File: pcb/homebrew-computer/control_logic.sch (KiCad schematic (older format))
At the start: 24 parts

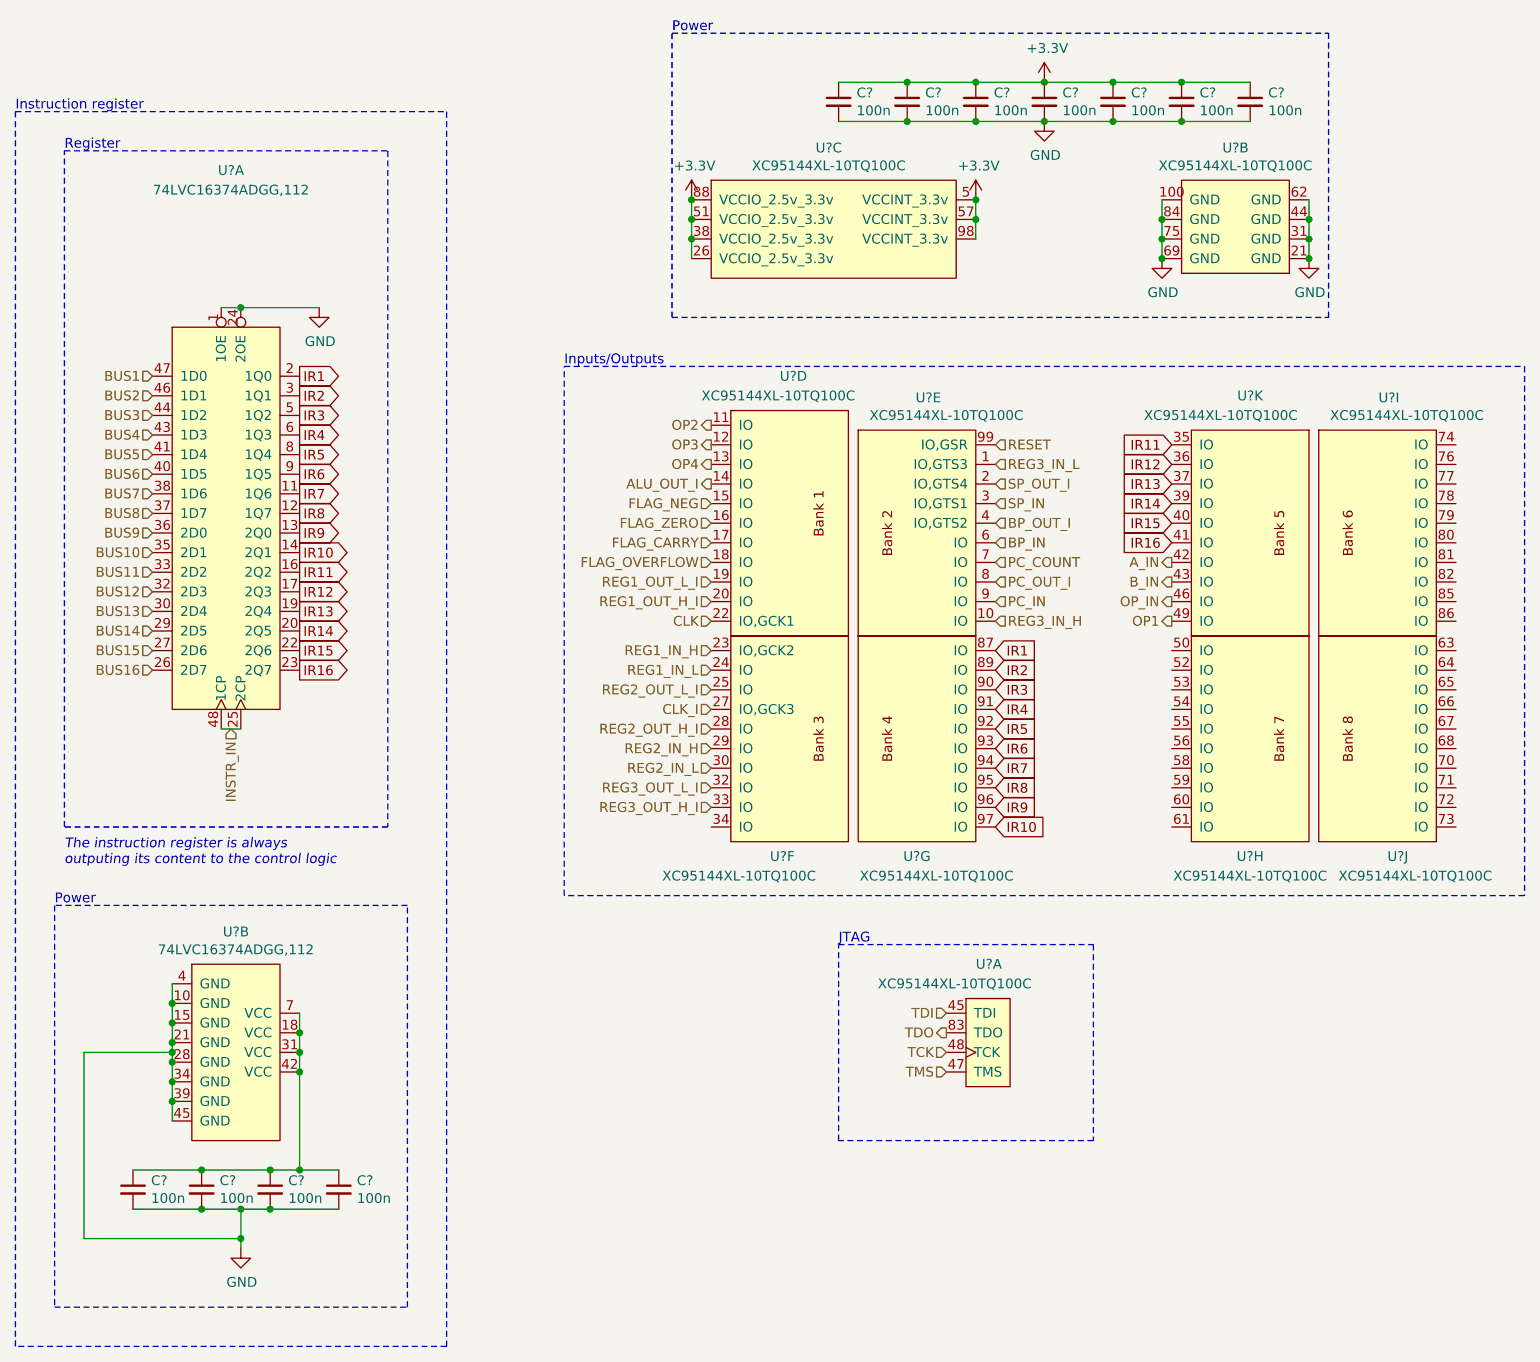
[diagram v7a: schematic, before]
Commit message: Connect signals between modules
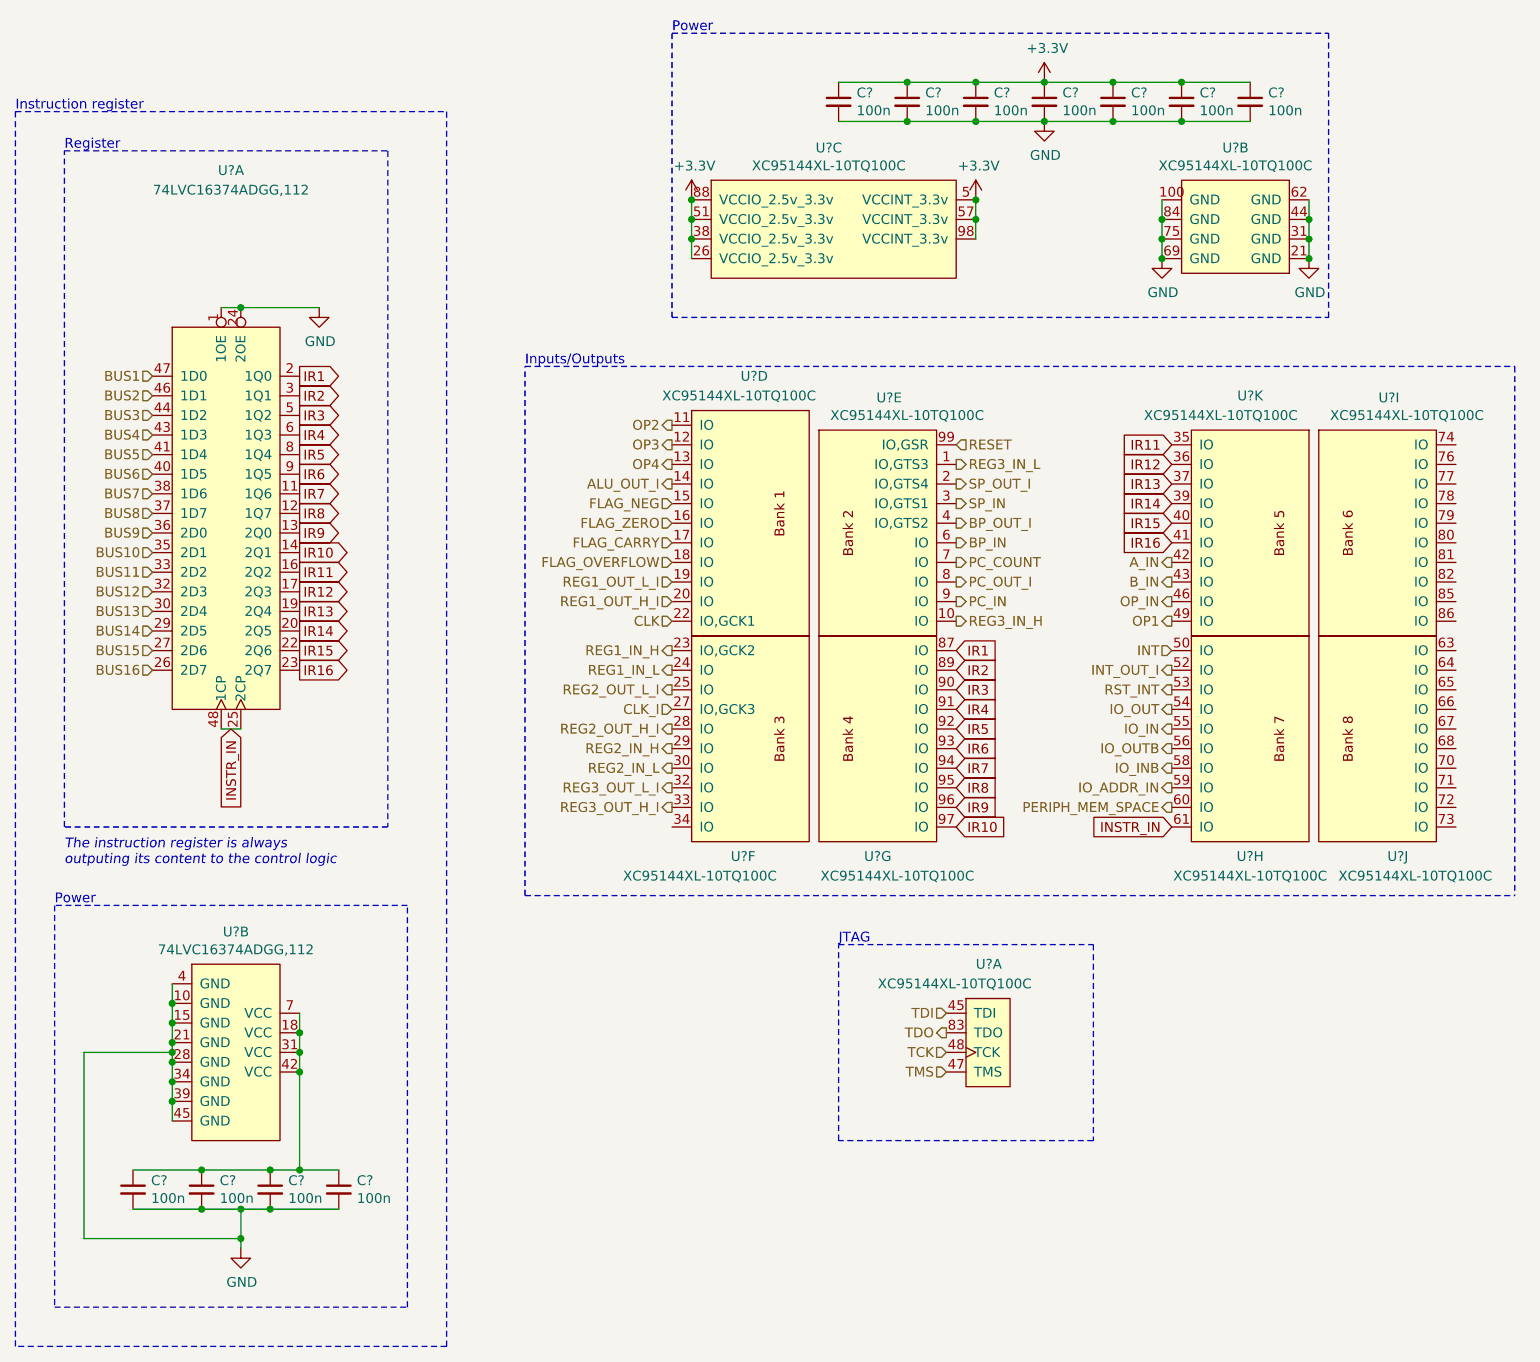
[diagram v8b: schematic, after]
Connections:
- net INSTR_IN: now also U?.61 (IO)
- net INT: now reaches U?.50 (IO)
- net INT_OUT_I: now reaches U?.52 (IO)
- net RST_INT: now reaches U?.53 (IO)
- net IO_OUT: now reaches U?.54 (IO)
- net IO_IN: now reaches U?.55 (IO)
- net IO_OUTB: now reaches U?.56 (IO)
- net IO_INB: now reaches U?.58 (IO)
- net IO_ADDR_IN: now reaches U?.59 (IO)
- net PERIPH_MEM_SPACE: now reaches U?.60 (IO)
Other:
- moved on the sheet: U?D, U?E, U?F, U?G
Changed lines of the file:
@@
 $Descr User 9449 8268
 encoding utf-8
-Sheet 7 7
+Sheet 6 7
 Title ""
 Date ""
@@
 Text Notes 5200 5300 0    50   ~ 0
 JTAG
-Text Notes 3800 2350 0    50   ~ 0
+Text Notes 3600 2350 0    50   ~ 0
 Inputs/Outputs
 $Comp
@@
 Wire Wire Line
 	2050 4200 2150 4200
-Text HLabel 2100 4200 3    50   Input ~ 0
-INSTR_IN
 Text HLabel 1700 2400 0    50   Input ~ 0
 BUS1
@@
 Text HLabel 6900 3650 0    50   Output ~ 0
 OP1
-Text HLabel 4550 2650 0    50   Output ~ 0
+Text HLabel 4350 2650 0    50   Output ~ 0
 OP2
-Text HLabel 4550 2750 0    50   Output ~ 0
+Text HLabel 4350 2750 0    50   Output ~ 0
 OP3
-Text HLabel 4550 2850 0    50   Output ~ 0
+Text HLabel 4350 2850 0    50   Output ~ 0
 OP4
-Text HLabel 4550 2950 0    50   Output ~ 0
+Text HLabel 4350 2950 0    50   Output ~ 0
 ALU_OUT_I
-Text HLabel 4550 3050 0    50   Input ~ 0
+Text HLabel 4350 3050 0    50   Input ~ 0
 FLAG_NEG
-Text HLabel 4550 3150 0    50   Input ~ 0
+Text HLabel 4350 3150 0    50   Input ~ 0
 FLAG_ZERO
-Text HLabel 4550 3250 0    50   Input ~ 0
+Text HLabel 4350 3250 0    50   Input ~ 0
 FLAG_CARRY
-Text HLabel 4550 3350 0    50   Input ~ 0
+Text HLabel 4350 3350 0    50   Input ~ 0
 FLAG_OVERFLOW
-Text HLabel 4550 3450 0    50   Input ~ 0
+Text HLabel 4350 3450 0    50   Input ~ 0
 REG1_OUT_L_I
-Text HLabel 4550 3550 0    50   Input ~ 0
+Text HLabel 4350 3550 0    50   Input ~ 0
 REG1_OUT_H_I
-Text HLabel 4550 3800 0    50   Input ~ 0
+Text HLabel 4350 3800 0    50   Output ~ 0
 REG1_IN_H
-Text HLabel 4550 3900 0    50   Input ~ 0
+Text HLabel 4350 3900 0    50   Output ~ 0
 REG1_IN_L
-Text HLabel 4550 4000 0    50   Input ~ 0
+Text HLabel 4350 4000 0    50   Output ~ 0
 REG2_OUT_L_I
-Text HLabel 4550 4200 0    50   Input ~ 0
+Text HLabel 4350 4200 0    50   Output ~ 0
 REG2_OUT_H_I
-Text HLabel 4550 4300 0    50   Input ~ 0
+Text HLabel 4350 4300 0    50   Output ~ 0
 REG2_IN_H
-Text HLabel 4550 4400 0    50   Input ~ 0
+Text HLabel 4350 4400 0    50   Output ~ 0
 REG2_IN_L
-Text HLabel 4550 4500 0    50   Input ~ 0
+Text HLabel 4350 4500 0    50   Output ~ 0
 REG3_OUT_L_I
-Text HLabel 4550 4600 0    50   Input ~ 0
+Text HLabel 4350 4600 0    50   Output ~ 0
 REG3_OUT_H_I
-Text HLabel 6000 3650 2    50   Input ~ 0
+Text HLabel 5800 3650 2    50   Output ~ 0
 REG3_IN_H
-Text HLabel 6000 2850 2    50   Input ~ 0
+Text HLabel 5800 2850 2    50   Output ~ 0
 REG3_IN_L
-Text HLabel 6000 2950 2    50   Input ~ 0
+Text HLabel 5800 2950 2    50   Output ~ 0
 SP_OUT_I
-Text HLabel 6000 3050 2    50   Input ~ 0
+Text HLabel 5800 3050 2    50   Output ~ 0
 SP_IN
-Text HLabel 6000 3150 2    50   Input ~ 0
+Text HLabel 5800 3150 2    50   Output ~ 0
 BP_OUT_I
-Text HLabel 6000 3250 2    50   Input ~ 0
+Text HLabel 5800 3250 2    50   Output ~ 0
 BP_IN
-Text HLabel 6000 3350 2    50   Input ~ 0
+Text HLabel 5800 3350 2    50   Output ~ 0
 PC_COUNT
-Text HLabel 6000 3450 2    50   Input ~ 0
+Text HLabel 5800 3450 2    50   Output ~ 0
 PC_OUT_I
-Text HLabel 6000 3550 2    50   Input ~ 0
+Text HLabel 5800 3550 2    50   Output ~ 0
 PC_IN
 $Comp
@@
 AR Path="/5F8B5CB7/5FA3E0E2" Ref="#PWR?"  Part="1"
 AR Path="/5F95DC76/5FA3E0E2" Ref="#PWR?"  Part="1"
-AR Path="/5F8B5E3D/5FA3E0E2" Ref="#PWR?"  Part="1"
-F 0 "#PWR?" H 7600 1550 50  0001 C CNN
+AR Path="/5F8B5E3D/5FA3E0E2" Ref="#PWR0142"  Part="1"
+F 0 "#PWR0142" H 7600 1550 50  0001 C CNN
 F 1 "GND" H 7605 1627 50  0000 C CNN
 F 2 "" H 7600 1800 50  0001 C CNN
@@
 AR Path="/5F8B5CB7/5FA5DEF3" Ref="#PWR?"  Part="1"
 AR Path="/5F95DC76/5FA5DEF3" Ref="#PWR?"  Part="1"
-AR Path="/5F8B5E3D/5FA5DEF3" Ref="#PWR?"  Part="1"
-F 0 "#PWR?" H 5900 1350 50  0001 C CNN
+AR Path="/5F8B5E3D/5FA5DEF3" Ref="#PWR0143"  Part="1"
+F 0 "#PWR0143" H 5900 1350 50  0001 C CNN
 F 1 "+3.3V" H 5915 1673 50  0000 C CNN
 F 2 "" H 5900 1500 50  0001 C CNN
@@
 AR Path="/5F8B5CB7/5FA6644B" Ref="#PWR?"  Part="1"
 AR Path="/5F95DC76/5FA6644B" Ref="#PWR?"  Part="1"
-AR Path="/5F8B5E3D/5FA6644B" Ref="#PWR?"  Part="1"
-F 0 "#PWR?" H 6250 750 50  0001 C CNN
+AR Path="/5F8B5E3D/5FA6644B" Ref="#PWR0144"  Part="1"
+F 0 "#PWR0144" H 6250 750 50  0001 C CNN
 F 1 "+3.3V" H 6265 1073 50  0000 C CNN
 F 2 "" H 6250 900 50  0001 C CNN
@@
 L XC9500XL:XC95144XL-10TQ100C U?
 U 4 1 5FA7DC14
-P 4650 2400
-F 0 "U?" H 4400 2400 50  0000 R CNN
-F 1 "XC95144XL-10TQ100C" H 4800 2300 50  0000 R CNN
-F 2 "" H 4650 2400 50  0001 C CNN
-F 3 "" H 4650 2400 50  0001 C CNN
-	4    4650 2400
+P 4450 2400
+F 0 "U?" H 4200 2400 50  0000 R CNN
+F 1 "XC95144XL-10TQ100C" H 4600 2300 50  0000 R CNN
+F 2 "" H 4450 2400 50  0001 C CNN
+F 3 "" H 4450 2400 50  0001 C CNN
+	4    4450 2400
 	-1   0    0    -1
 $EndComp
@@
 L XC9500XL:XC95144XL-10TQ100C U?
 U 6 1 5FA858A3
-P 4850 3600
-F 0 "U?" H 4850 2350 50  0000 R CNN
-F 1 "XC95144XL-10TQ100C" H 5400 2250 50  0000 R CNN
-F 2 "" H 4850 3600 50  0001 C CNN
-F 3 "" H 4850 3600 50  0001 C CNN
-	6    4850 3600
+P 4650 3600
+F 0 "U?" H 4650 2350 50  0000 R CNN
+F 1 "XC95144XL-10TQ100C" H 5200 2250 50  0000 R CNN
+F 2 "" H 4650 3600 50  0001 C CNN
+F 3 "" H 4650 3600 50  0001 C CNN
+	6    4650 3600
 	-1   0    0    -1
 $EndComp
@@
 	-1   0    0    -1
 $EndComp
-Text HLabel 4550 3650 0    50   Input ~ 0
+Text HLabel 4350 3650 0    50   Input ~ 0
 CLK
-Text HLabel 4550 4100 0    50   Input ~ 0
+Text HLabel 4350 4100 0    50   Input ~ 0
 CLK_I
 $Comp
@@
 L XC9500XL:XC95144XL-10TQ100C U?
 U 5 1 5FADBDB0
-P 5900 2500
-F 0 "U?" H 5658 2490 50  0000 C CNN
-F 1 "XC95144XL-10TQ100C" H 5750 2400 50  0000 C CNN
-F 2 "" H 5900 2475 50  0001 C CNN
-F 3 "" H 5900 2475 50  0001 C CNN
-	5    5900 2500
+P 5700 2500
+F 0 "U?" H 5458 2490 50  0000 C CNN
+F 1 "XC95144XL-10TQ100C" H 5550 2400 50  0000 C CNN
+F 2 "" H 5700 2475 50  0001 C CNN
+F 3 "" H 5700 2475 50  0001 C CNN
+	5    5700 2500
 	1    0    0    -1
 $EndComp
@@
 L XC9500XL:XC95144XL-10TQ100C U?
 U 7 1 5FA897E9
-P 5700 3600
-F 0 "U?" H 5600 2350 50  0000 C CNN
-F 1 "XC95144XL-10TQ100C" H 5700 2250 50  0000 C CNN
-F 2 "" H 5700 3600 50  0001 C CNN
-F 3 "" H 5700 3600 50  0001 C CNN
-	7    5700 3600
-	1    0    0    -1
-$EndComp
-Text GLabel 6000 4700 2    50   Input ~ 0
+P 5500 3600
+F 0 "U?" H 5400 2350 50  0000 C CNN
+F 1 "XC95144XL-10TQ100C" H 5500 2250 50  0000 C CNN
+F 2 "" H 5500 3600 50  0001 C CNN
+F 3 "" H 5500 3600 50  0001 C CNN
+	7    5500 3600
+	1    0    0    -1
+$EndComp
+Text GLabel 5800 4700 2    50   Input ~ 0
 IR10
-Text GLabel 6000 4600 2    50   Input ~ 0
+Text GLabel 5800 4600 2    50   Input ~ 0
 IR9
-Text GLabel 6000 4500 2    50   Input ~ 0
+Text GLabel 5800 4500 2    50   Input ~ 0
 IR8
-Text GLabel 6000 4400 2    50   Input ~ 0
+Text GLabel 5800 4400 2    50   Input ~ 0
 IR7
-Text GLabel 6000 4300 2    50   Input ~ 0
+Text GLabel 5800 4300 2    50   Input ~ 0
 IR6
-Text GLabel 6000 4200 2    50   Input ~ 0
+Text GLabel 5800 4200 2    50   Input ~ 0
 IR5
-Text GLabel 6000 4100 2    50   Input ~ 0
+Text GLabel 5800 4100 2    50   Input ~ 0
 IR4
-Text GLabel 6000 4000 2    50   Input ~ 0
+Text GLabel 5800 4000 2    50   Input ~ 0
 IR3
-Text GLabel 6000 3900 2    50   Input ~ 0
+Text GLabel 5800 3900 2    50   Input ~ 0
 IR2
-Text GLabel 6000 3800 2    50   Input ~ 0
+Text GLabel 5800 3800 2    50   Input ~ 0
 IR1
 $Comp
@@
 	1    0    0    -1
 $EndComp
-Text HLabel 6000 2750 2    50   Input ~ 0
+Text HLabel 5800 2750 2    50   Input ~ 0
 RESET
 Wire Notes Line
-	8700 2350 8700 5050
-Wire Notes Line
-	8700 5050 3800 5050
-Wire Notes Line
-	3800 5050 3800 2350
-Wire Notes Line
-	3800 2350 8700 2350
+	3600 5050 3600 2350
 $Comp
 L power:GND #PWR?
@@
 AR Path="/5F8C07F0/5FB4050E" Ref="#PWR?"  Part="1"
 AR Path="/5F95DC76/5FB4050E" Ref="#PWR?"  Part="1"
-AR Path="/5F8B5E3D/5FB4050E" Ref="#PWR?"  Part="1"
-F 0 "#PWR?" H 2550 1800 50  0001 C CNN
+AR Path="/5F8B5E3D/5FB4050E" Ref="#PWR0145"  Part="1"
+F 0 "#PWR0145" H 2550 1800 50  0001 C CNN
 F 1 "GND" H 2555 1877 50  0000 C CNN
 F 2 "" H 2550 2050 50  0001 C CNN
@@
 Text Notes 1250 4900 0    50   Italic 0
 The instruction register is always\noutputing its content to the control logic
+Text HLabel 6900 3800 0    50   Input ~ 0
+INT
+Text HLabel 6900 3900 0    50   Output ~ 0
+INT_OUT_I
+Text HLabel 6900 4000 0    50   Output ~ 0
+RST_INT
+Text HLabel 6900 4100 0    50   Output ~ 0
+IO_OUT
+Text HLabel 6900 4200 0    50   Output ~ 0
+IO_IN
+Text HLabel 6900 4300 0    50   Output ~ 0
+IO_OUTB
+Text HLabel 6900 4400 0    50   Output ~ 0
+IO_INB
+Text HLabel 6900 4500 0    50   Output ~ 0
+IO_ADDR_IN
+Text HLabel 6900 4600 0    50   Output ~ 0
+PERIPH_MEM_SPACE
+Wire Notes Line
+	8650 2350 8650 5050
+Wire Notes Line
+	3600 5050 8650 5050
+Wire Notes Line
+	3600 2350 8650 2350
+Text GLabel 2100 4200 3    50   Input ~ 0
+INSTR_IN
+Text GLabel 6900 4700 0    50   Input ~ 0
+INSTR_IN
 $EndSCHEMATC
